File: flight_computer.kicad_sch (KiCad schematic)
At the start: 25 parts, among them J1 Conn_01x13_Socket, J2 Conn_01x13_Socket, J3 Ignitor Output, J4 Battery Input, U1 CPC1002N, U2 CPC1002N, U3 CPC1002N, U4 BME280, U5 BNO055, U6 TPS62172DSG, Y1 33.768kHz

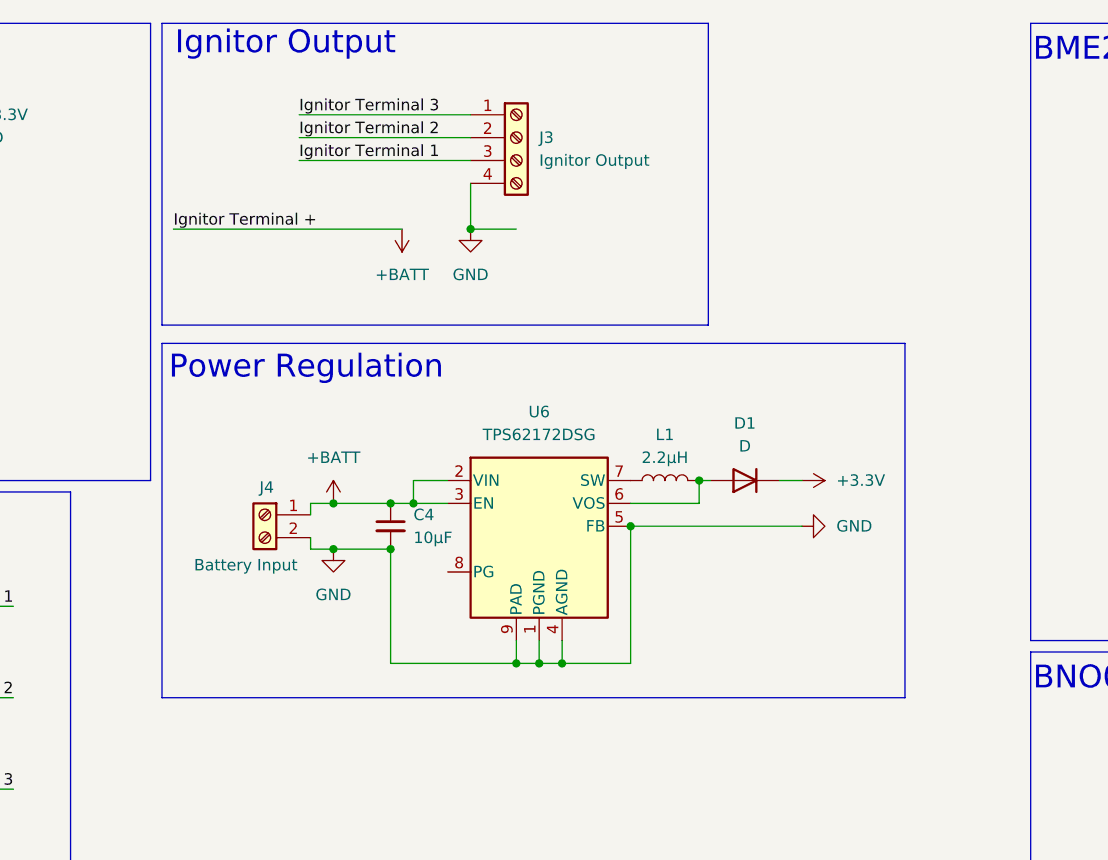
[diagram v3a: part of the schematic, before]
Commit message: Improved layout of connectors
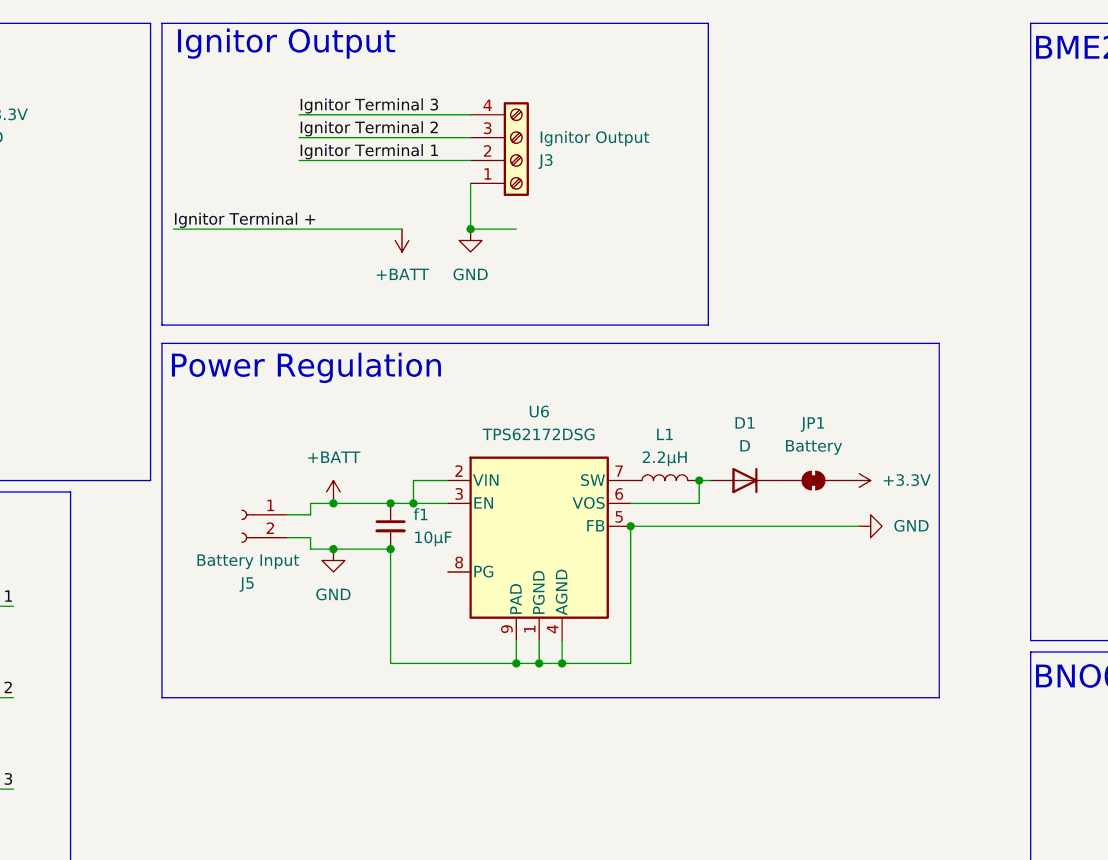
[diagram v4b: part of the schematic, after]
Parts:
- removed J4: Battery Input, TerminalBlock_Phoenix:TerminalBlock_Phoenix_MPT-0,5-2-2.54_1x02_P2.54mm_Horizontal, symbol Connector:Screw_Terminal_01x02
- added J5: Battery Input, Connector_JST:JST_PH_S2B-PH-K_1x02_P2.00mm_Horizontal, symbol Connector:Conn_01x02_Socket
- added JP1: Battery, Jumper:SolderJumper-2_P1.3mm_Bridged_Pad1.0x1.5mm, symbol Jumper:SolderJumper_2_Bridged
- f1: renamed from C4; footprint Capacitor_SMD:C_0603_1608Metric_Pad1.08x0.95mm_HandSolder -> Capacitor_SMD:C_0805_2012Metric_Pad1.18x1.45mm_HandSolder
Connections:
- net +3.3V: now also JP1.2 (B); no longer D1.1 (K)
- net +BATT: now also J5.1 (Pin_1)
- net GND: now also J3.1 (Pin_1), J5.2 (Pin_2); no longer J3.4 (Pin_4)
- net Ignitor Terminal 1: now also J3.2 (Pin_2); no longer J3.3 (Pin_3)
- net Ignitor Terminal 2: now also J3.3 (Pin_3); no longer J3.2 (Pin_2)
- net Ignitor Terminal 3: now also J3.4 (Pin_4); no longer J3.1 (Pin_1)
- new net: D1.1 (K), JP1.1 (A)
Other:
- title: (none) -> UNL Aerospace Flight Computer

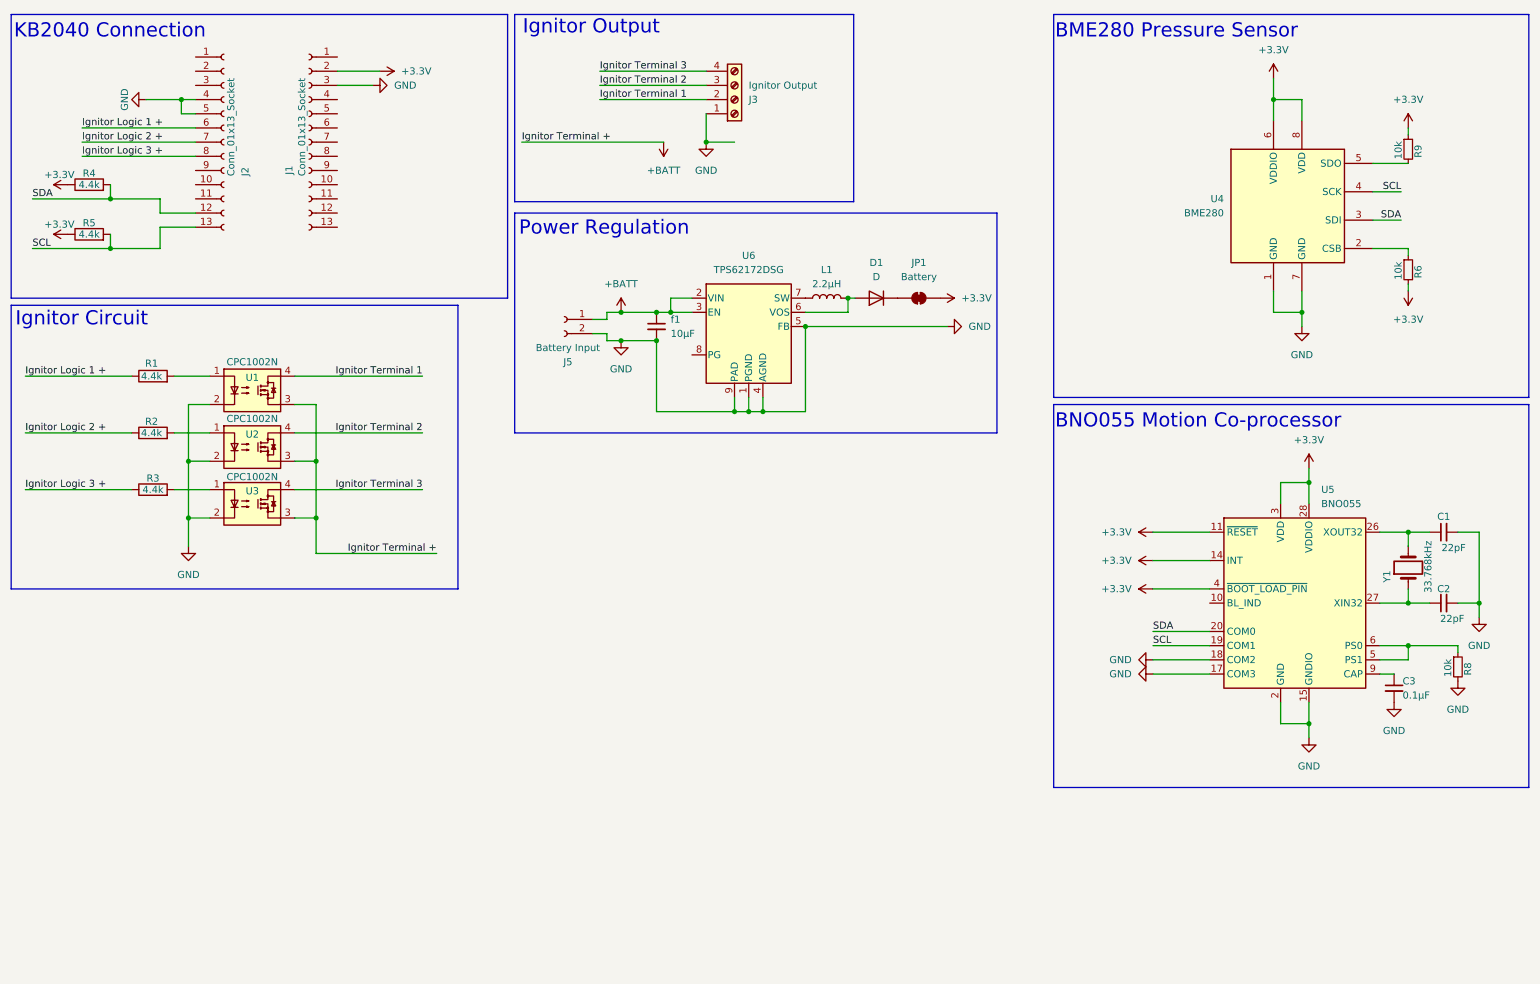
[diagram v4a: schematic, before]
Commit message: Added MicroSD card slot
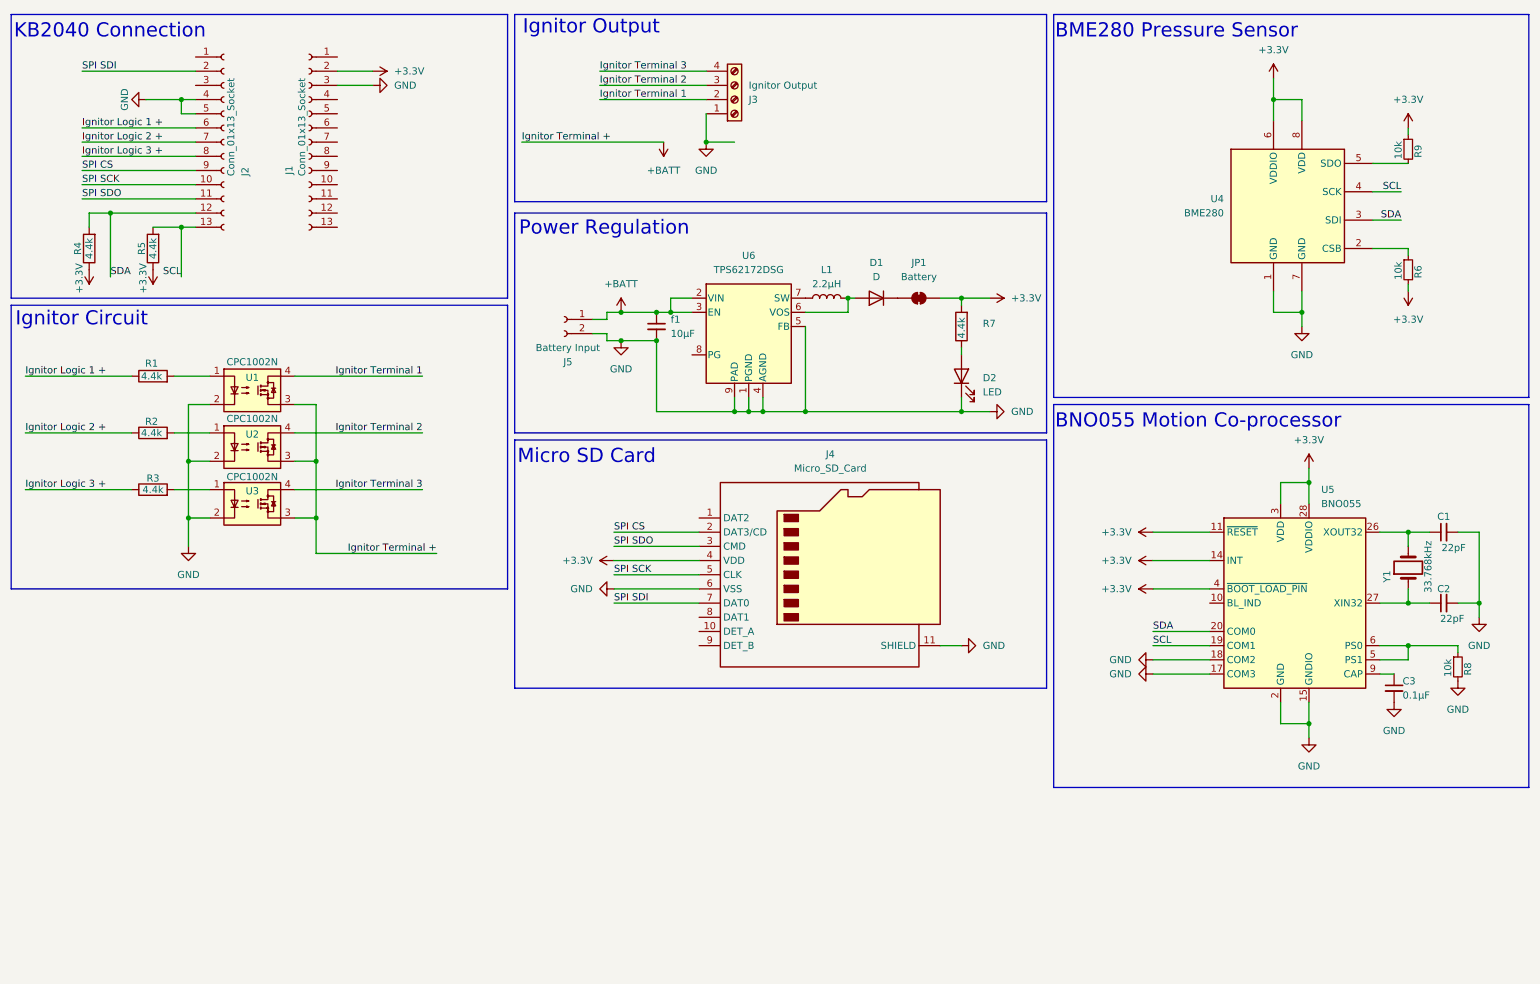
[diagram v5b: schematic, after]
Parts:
- added D2: LED, LED_SMD:LED_0603_1608Metric_Pad1.05x0.95mm_HandSolder, symbol Device:LED
- added J4: Micro_SD_Card, Connector_Card:microSD_HC_Hirose_DM3D-SF, symbol Connector:Micro_SD_Card_Det_Hirose_DM3AT
- added R7: 4.4k, Resistor_SMD:R_0603_1608Metric_Pad0.98x0.95mm_HandSolder, symbol Device:R
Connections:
- net +3.3V: now also J4.4 (VDD), R7.2
- net GND: now also D2.1 (K), J4.11 (SHIELD), J4.6 (VSS)
- net SPI SCK: now reaches J2.10 (Pin_10)
- net SPI SCK: now also J4.5 (CLK)
- net SPI SDO: now reaches J2.11 (Pin_11)
- net SPI SDO: now also J4.3 (CMD)
- net SPI SDI: now reaches J2.2 (Pin_2)
- net SPI SDI: now also J4.7 (DAT0)
- net SPI CS: now reaches J2.9 (Pin_9)
- net SPI CS: now also J4.2 (DAT3/CD)
- new net: D2.2 (A), R7.1
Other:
- note added: "Micro SD Card"
- moved on the sheet: R4, R5

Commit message: Added inter-board connectors to i2c
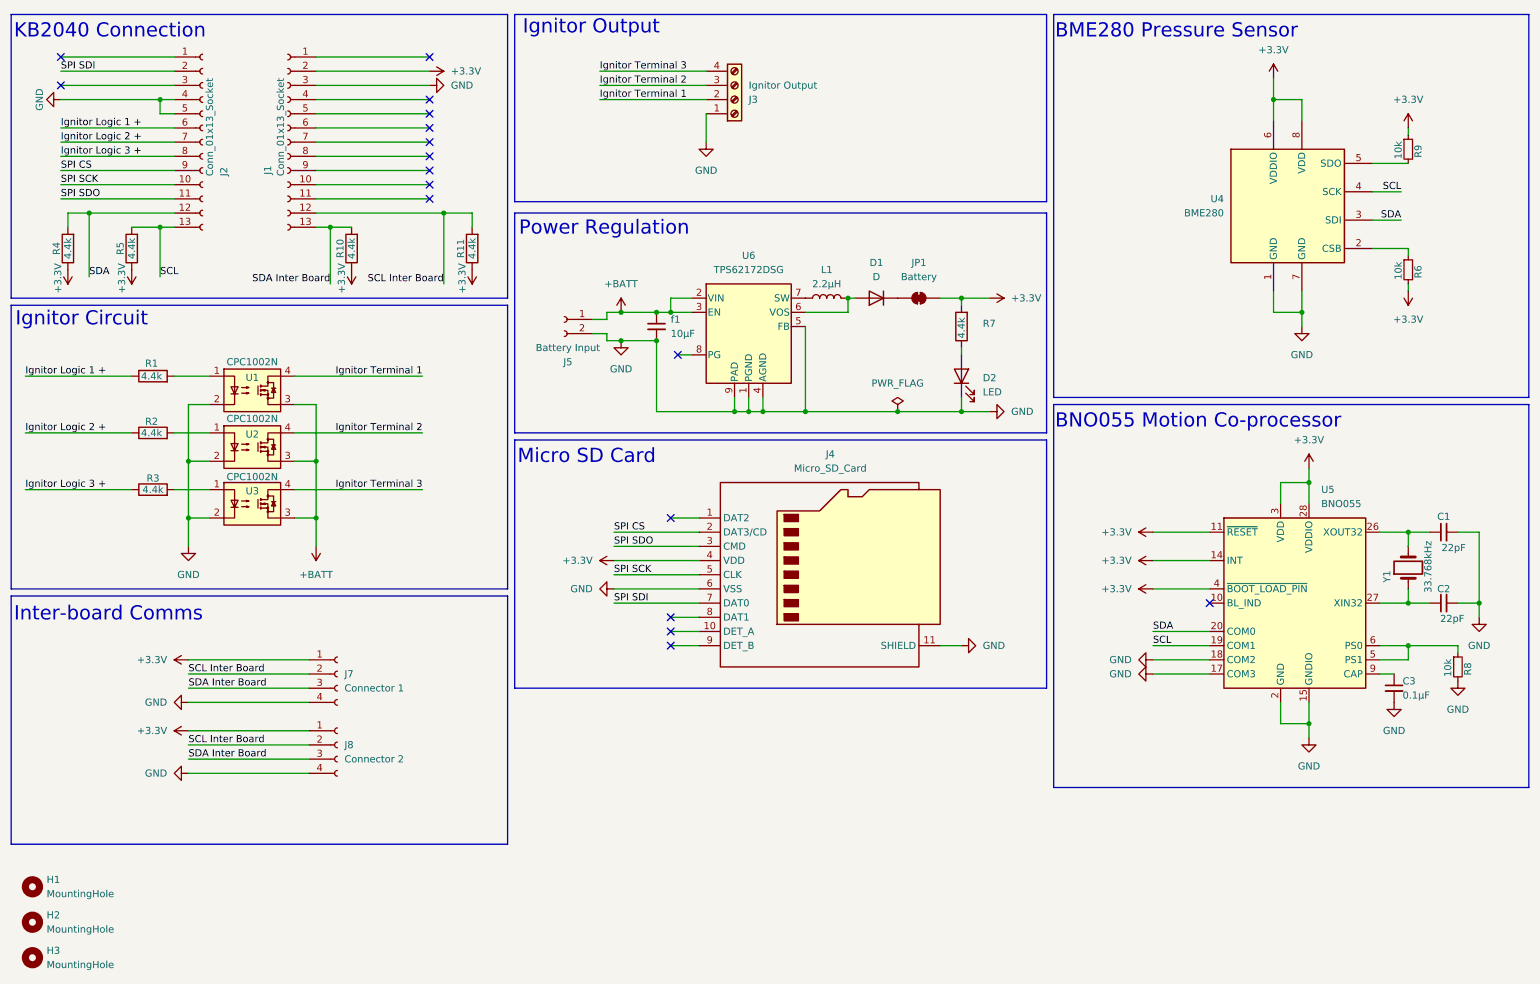
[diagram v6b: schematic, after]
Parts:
- added H1, H2, H3: MountingHole, MountingHole:MountingHole_2.2mm_M2_ISO7380, symbol Mechanical:MountingHole
- added J7: Connector 1, Connector_Molex:Molex_PicoBlade_53047-0410_1x04_P1.25mm_Vertical, symbol Connector:Conn_01x04_Socket
- added J8: Connector 2, Connector_Molex:Molex_PicoBlade_53047-0410_1x04_P1.25mm_Vertical, symbol Connector:Conn_01x04_Socket
- added R10, R11: 4.4k, Resistor_SMD:R_0603_1608Metric_Pad0.98x0.95mm_HandSolder, symbol Device:R
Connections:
- net +3.3V: now also J7.1 (Pin_1), J8.1 (Pin_1), R10.1, R11.1
- net GND: now also J7.4 (Pin_4), J8.4 (Pin_4)
- net SCL Inter Board: now reaches J1.12 (Pin_12)
- net SCL Inter Board: now also J7.2 (Pin_2), J8.2 (Pin_2), R11.2
- net SDA Inter Board: now reaches J1.13 (Pin_13)
- net SDA Inter Board: now also J7.3 (Pin_3), J8.3 (Pin_3), R10.2
- no-connect marks 0 -> 17
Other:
- note added: "Inter-board Comms"
- moved on the sheet: J1, J2, R4, R5
